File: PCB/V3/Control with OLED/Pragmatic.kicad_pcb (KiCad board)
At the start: 2 copper layers, 41.9 x 48.3 mm, 8 parts, among them J1 L, J2 R, J3 Conn_01x04, SW1 SW_Push, U1 ProMicro

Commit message: prepare for manufacture
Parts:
- added J4: OLED, Keyboard_JSA:SSD1306_OLED-0.91-128x32, F.Cu at (157.5, 93.3)
- J3: value Conn_01x04 -> OLED
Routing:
- net Row1: track 66.0 -> 108.6 mm
- net Row2: track 71.6 -> 106.0 mm
- net VCC: track 93.7 -> 101.6 mm, vias 0 -> 1
- net GND: track 108.8 -> 112.4 mm

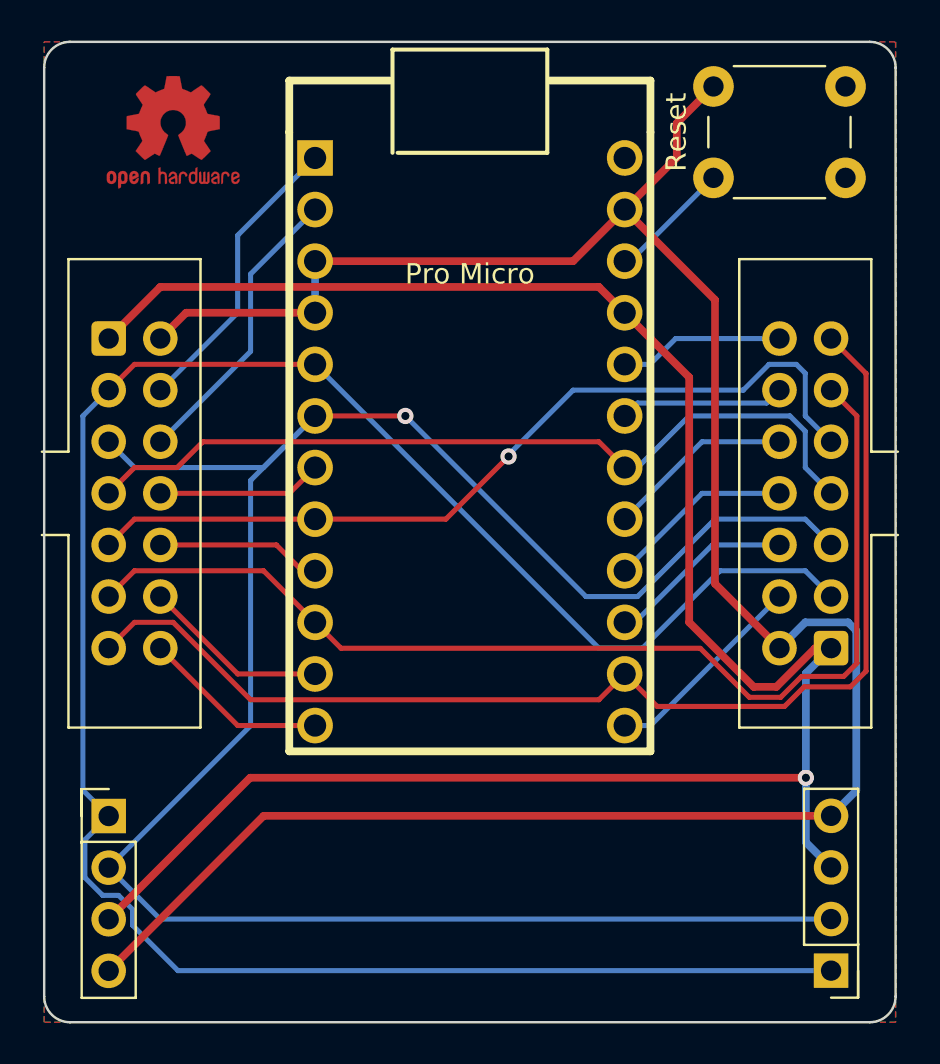
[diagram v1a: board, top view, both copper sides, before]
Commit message: reversed pro micro
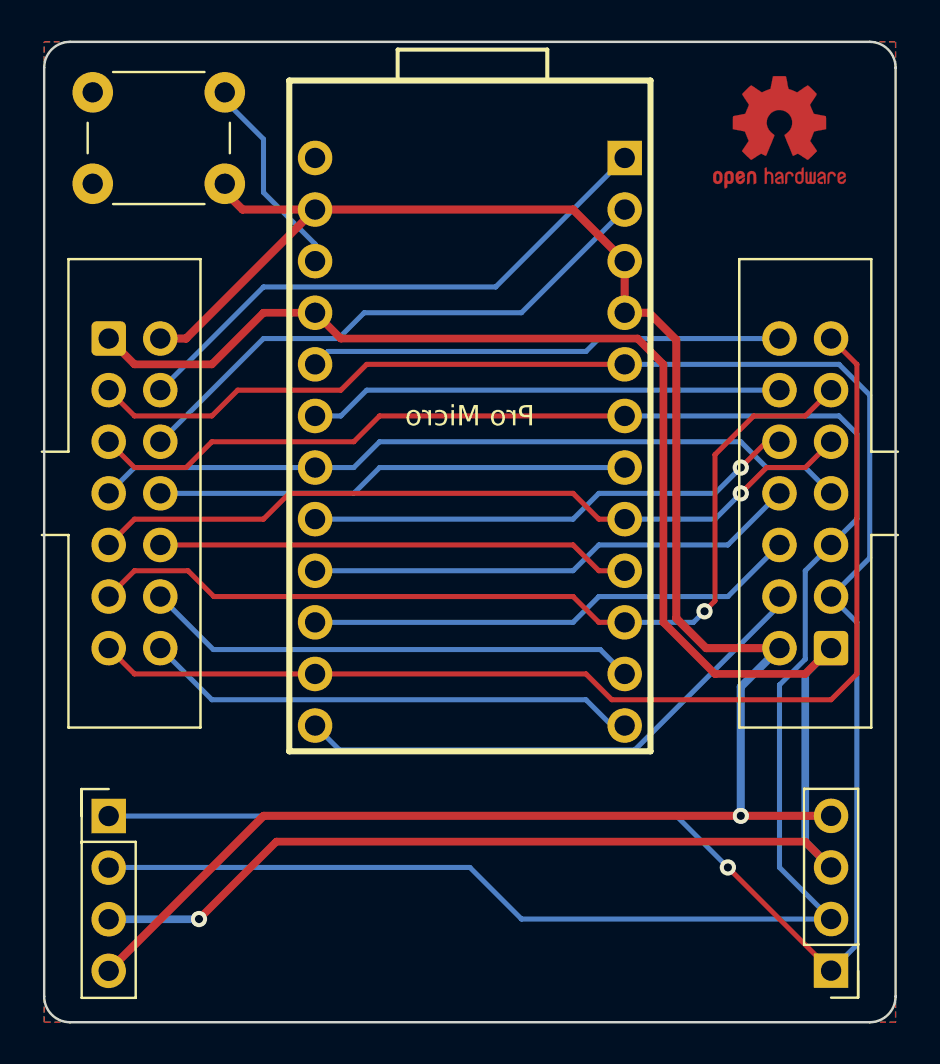
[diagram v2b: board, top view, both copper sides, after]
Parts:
- removed REF**: KiCad-Logo_5mm_SilkScreen, Symbol:KiCad-Logo_5mm_SilkScreen
- U1: footprint Keyboard_JSA:ArduinoProMicro -> Keyboard_JSA:ProMicro Reversed; moved to B.Cu
- moved SW1 37.3 mm to (121.1, 50.1), turned to 0 degrees
- moved Logo1 29.8 mm to (154.9, 52.1)
- moved U1 1.27 mm to (139.7, 66.0), turned to 180 degrees
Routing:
- net Col7: track 10.3 -> 26.7 mm
- net Col5: track 9.20 -> 24.4 mm
- net Col3: track 8.15 -> 23.4 mm
- net Col8: track 9.20 -> 24.4 mm
- net Col11: track 8.15 -> 23.4 mm
- net Col9: track 9.20 -> 24.4 mm
- net Col6: track 9.20 -> 24.4 mm
- net Col10: track 9.20 -> 24.4 mm, vias 0 -> 1
- net Col4: track 8.15 -> 23.4 mm
- net Col12: track 8.15 -> 23.4 mm
- net Col2: track 14.6 -> 27.6 mm
- net Col1: track 14.6 -> 27.6 mm
- net Row5: track 54.6 -> 46.1 mm, vias 0 -> 1
- net GND: track 112.4 -> 104.5 mm, vias 0 -> 1
- net Row2: track 106.0 -> 101.9 mm, vias 1 -> 0
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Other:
- board text added: "1"
- board text added: "10"
- board text added: "11"
- board text added: "12"
- board text added: "2"
- board text added: "3"
- board text added: "4"
- board text added: "5"
- board text added: "6"
- board text added: "7"
- board text added: "8"
- board text added: "9"
- board text added: "Col"
- board text added: "Pragmatic Keyboard Kit Control Module V3.2 https://github.com/ jamessa/Pragmatic"
- board text added: "Row"
- board text removed: "Pragmatic Keyboard Kit Control Module Design by James Sa V3.1 2022-06-13"
- board text removed: "Pro Micro"

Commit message: fix silk screen
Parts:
- added REF**: KiCad-Logo_5mm_Copper, Symbol:KiCad-Logo_5mm_Copper, B.Cu at (153.7, 53.3)
- moved L1 42.6 mm to (139.7, 89.5)
